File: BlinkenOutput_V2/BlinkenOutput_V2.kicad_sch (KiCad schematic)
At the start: 27 parts, among them J1 Conn_01x10, J2 Conn_01x10, J3 Conn_02x07_Odd_Even, J4 Conn_02x02_Counter_Clockwise, J5 Conn_02x02_Counter_Clockwise, U1 LTV-847S, U2 LTV-847S, U3 74HC595, U4 74LVC1G125

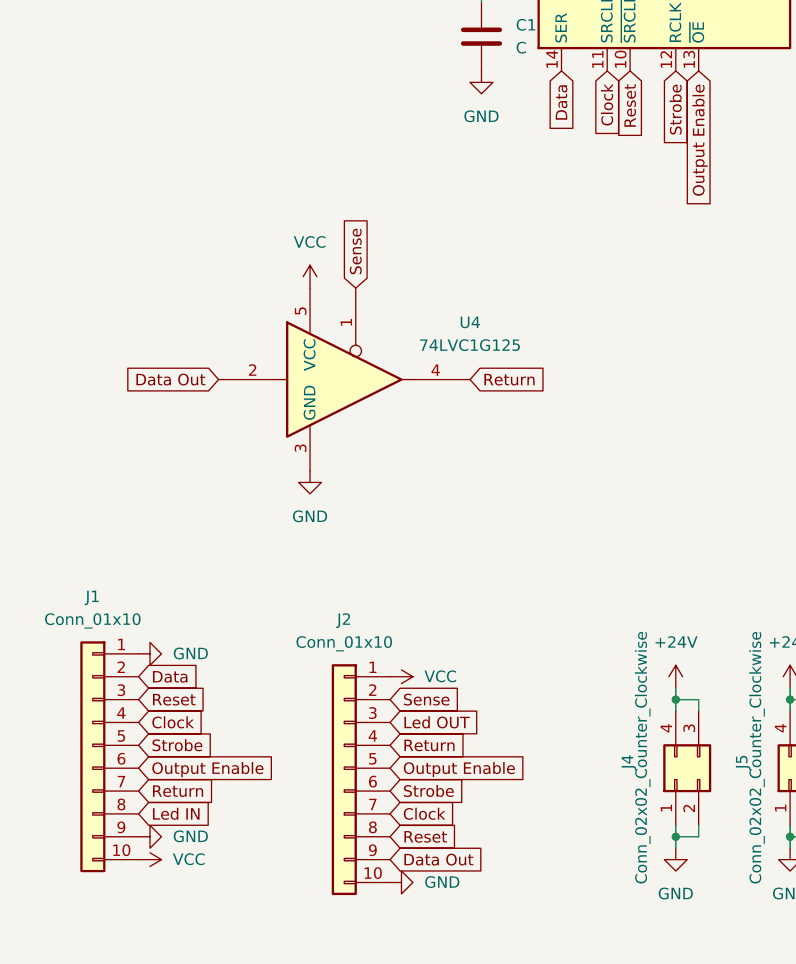
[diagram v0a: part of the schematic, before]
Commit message: Overhauled the output board
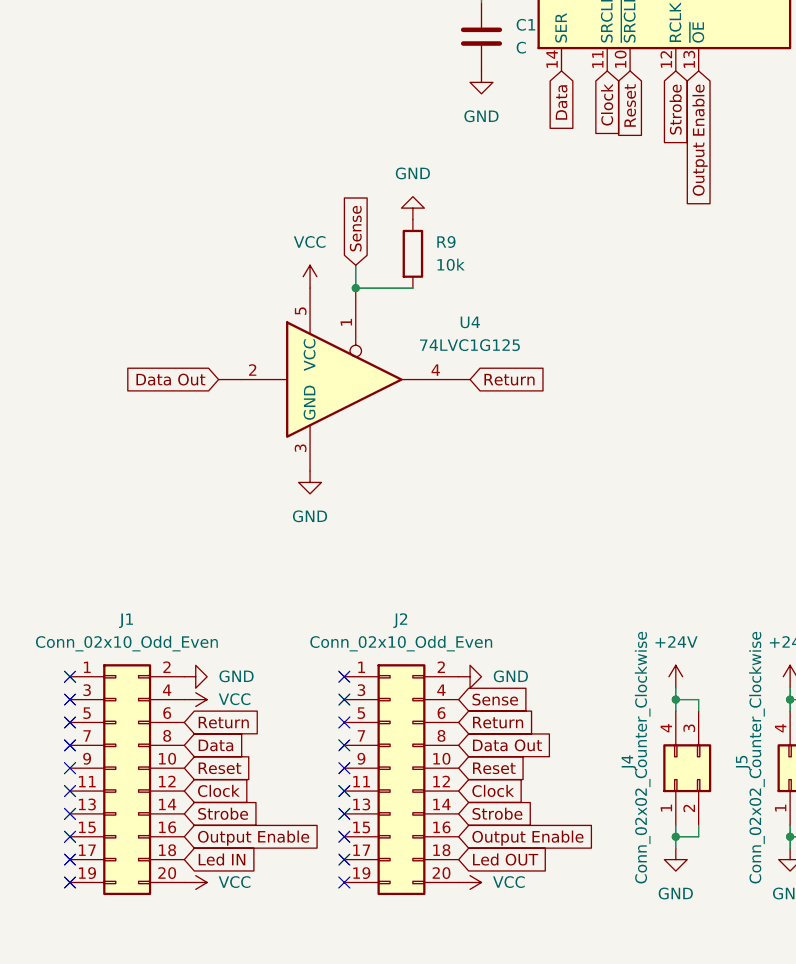
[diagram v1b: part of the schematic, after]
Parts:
- removed J1: Conn_01x10, Connector_PinHeader_2.54mm:PinHeader_1x10_P2.54mm_Vertical_SMD_Pin1Left, symbol Connector_Generic:Conn_01x10
- removed J2: Conn_01x10, Connector_PinSocket_2.54mm:PinSocket_1x10_P2.54mm_Vertical_SMD_Pin1Left, symbol Connector_Generic:Conn_01x10
- added J1: Conn_02x10_Odd_Even, Connector_PinSocket_2.54mm:PinSocket_2x10_P2.54mm_Vertical_SMD, symbol Connector_Generic:Conn_02x10_Odd_Even
- added J2: Conn_02x10_Odd_Even, Connector_PinHeader_2.54mm:PinHeader_2x10_P2.54mm_Vertical_SMD, symbol Connector_Generic:Conn_02x10_Odd_Even
- added R9: 10k, Resistor_SMD:R_0805_2012Metric_Pad1.20x1.40mm_HandSolder, symbol Device:R
- J4: footprint Connector_PinHeader_2.00mm:PinHeader_2x02_P2.00mm_Vertical_SMD -> Connector_PinHeader_2.54mm:PinHeader_2x02_P2.54mm_Vertical_SMD
- J5: footprint Connector_PinSocket_2.00mm:PinSocket_2x02_P2.00mm_Vertical_SMD -> Connector_PinSocket_2.54mm:PinSocket_2x02_P2.54mm_Vertical_SMD
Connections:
- net Clock: now also J1.12 (Pin_12), J2.12 (Pin_12)
- net Data: now also J1.8 (Pin_8)
- net Data Out: now also J2.8 (Pin_8)
- net GND: now also J1.2 (Pin_2), J2.2 (Pin_2), R9.1
- net Led IN: now also J1.18 (Pin_18)
- net Led OUT: now also J2.18 (Pin_18)
- net Output Enable: now also J1.16 (Pin_16), J2.16 (Pin_16)
- net Reset: now also J1.10 (Pin_10), J2.10 (Pin_10)
- net Return: now also J1.6 (Pin_6), J2.6 (Pin_6)
- net Sense: now also J2.4 (Pin_4), R9.2
- net Strobe: now also J1.14 (Pin_14), J2.14 (Pin_14)
- net VCC: now also J1.20 (Pin_20), J1.4 (Pin_4), J2.20 (Pin_20)
- no-connect marks 0 -> 20
